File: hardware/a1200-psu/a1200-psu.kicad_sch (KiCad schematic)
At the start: 60 parts, among them J2 Conn_01x05, U1 PC817

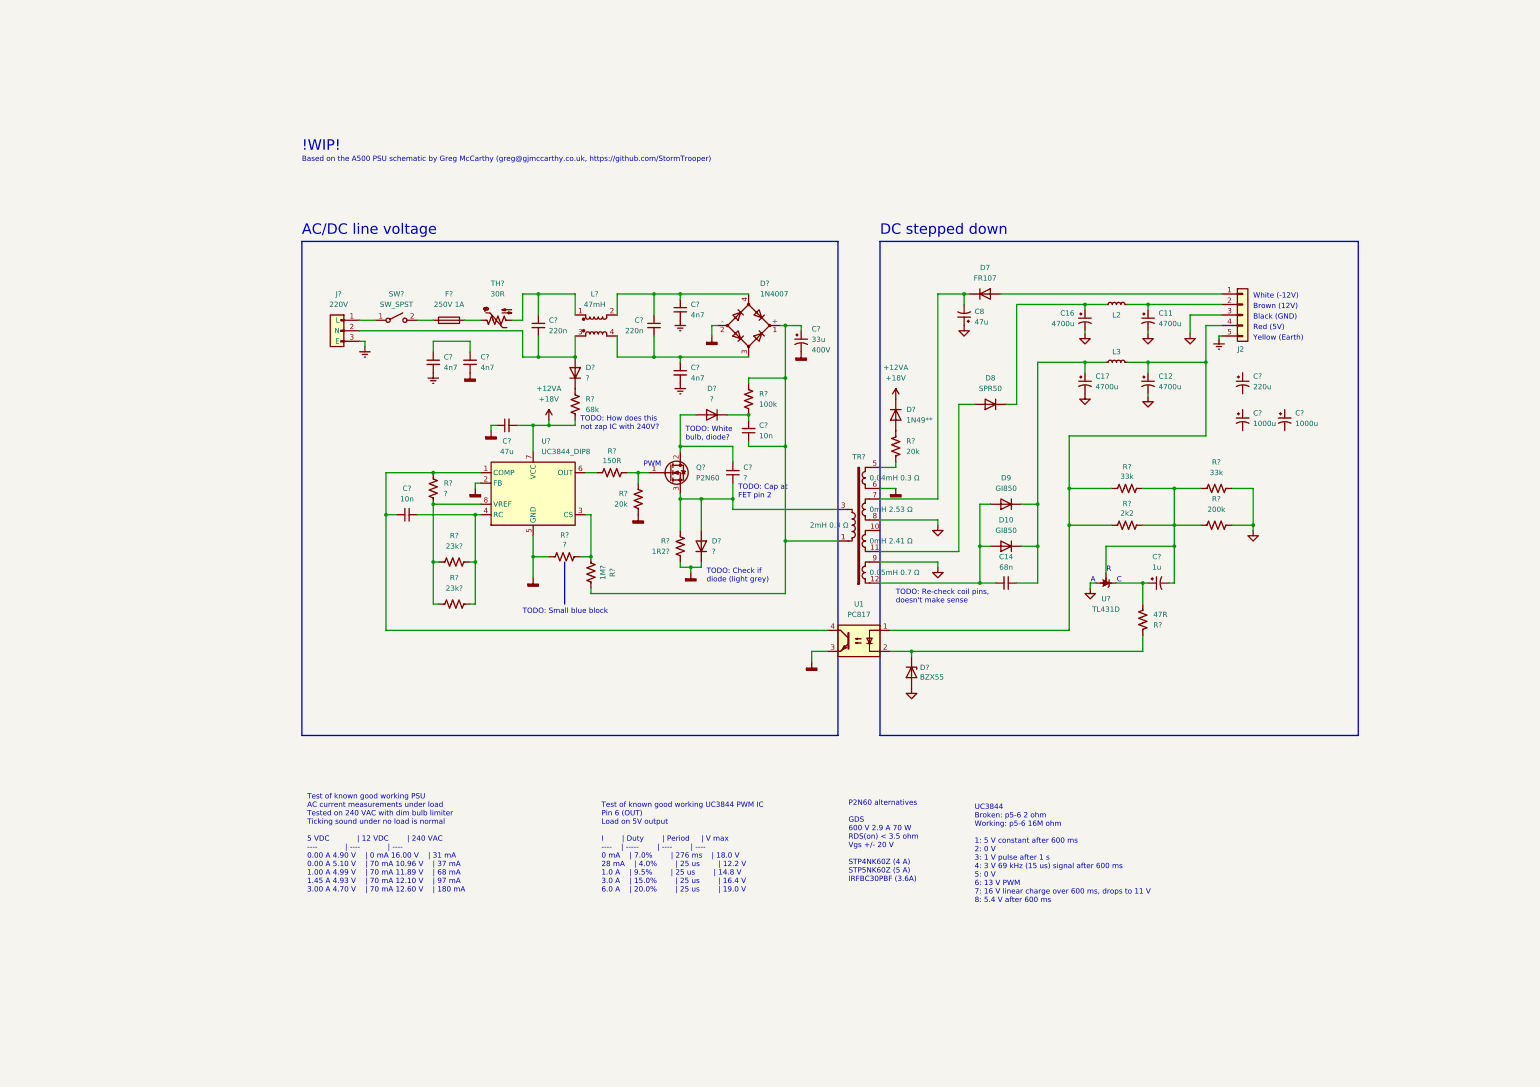
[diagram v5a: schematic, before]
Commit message: Fixed transformer wiring
Also corrected cap values
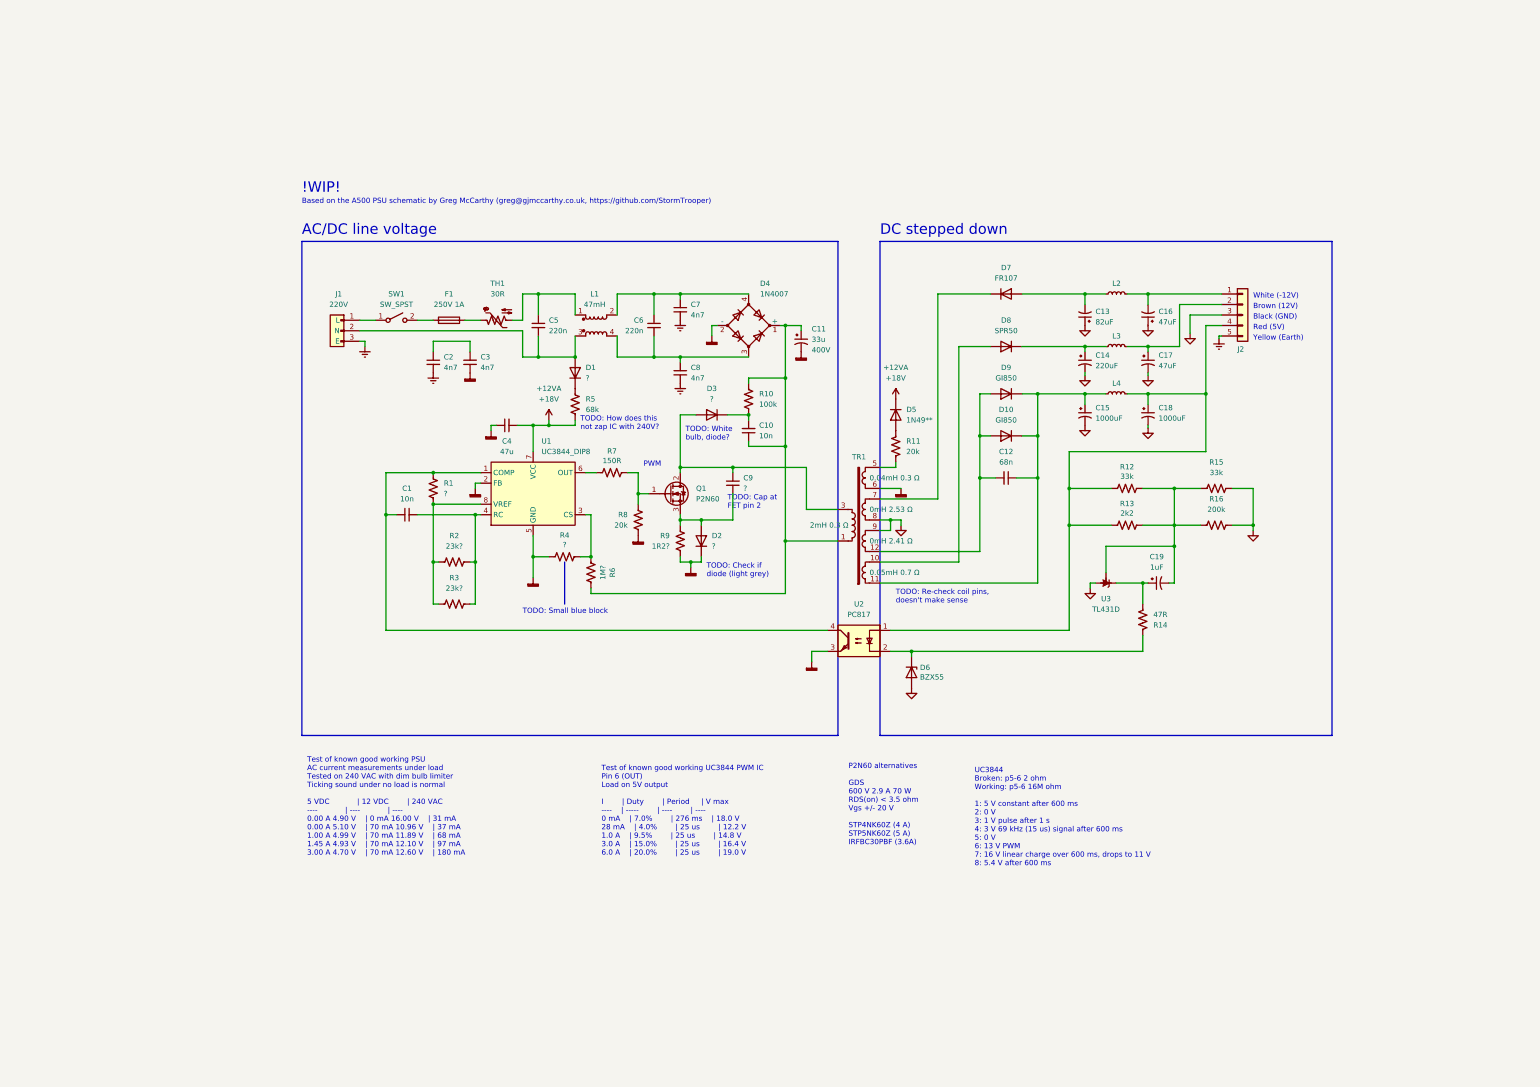
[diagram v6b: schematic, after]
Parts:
- removed C12, C17: 4700u, symbol a500-psu-rescue:CP1_Small-Device
- removed C8: 47u, symbol a500-psu-rescue:CP1_Small-Device
- removed C?: 220u, symbol a500-psu-rescue:CP1_Small-Device
- removed C? (x2): 1000u, symbol a500-psu-rescue:CP1_Small-Device
- added C13: 82uF, symbol a500-psu-rescue:CP1_Small-Device
- added C15, C18: 1000uF, symbol a500-psu-rescue:CP1_Small-Device
- added C16: 47uF, symbol a500-psu-rescue:CP1_Small-Device
- added L2: L_Small, symbol Device:L_Small
- C14: renamed from C16; value 4700u -> 220uF
- C17: renamed from C11; value 4700u -> 47uF
- C19: renamed from C?; value 1u -> 1uF
- U3: renamed from U?; symbol Reference_Voltage:TL431D -> Amiga 1200:TL431D
- gave numbers to parts that had none: 41
- renumbered C14 to C12, L2 to L3, L3 to L4, U1 to U2
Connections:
- net GND: now also C13.1, C15.2, C16.1, C18.2
- net at J2.1 (Pin_1): now also C16.2, L2.2; no longer D7.2 (A)
- net at J2.4 (Pin_4), L4.2, R12.2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: now also C18.1
- net at D8.2 (A): now also TR1.10; no longer TR1.11
- net at C12.1, D10.1 (K), D9.1 (K)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: now also TR1.11, C15.1
- net at C9.1, D2.2 (A), Q1.3 (S)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: no longer TR1.3
- net at C9.2, D3.2 (A), Q1.2 (D): now also TR1.3
- new net: C13.2, D7.2 (A), L2.1
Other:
- note removed: "A"
- note removed: "C"
- note removed: "R"
- title: Amiga A1200 PSU UK 391029-02 -> Amiga A1200 PSU (UK)
- moved on the sheet: C12, C14, C17, C9, D10, D2, D7, D8, D9, L3, L4, Q1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

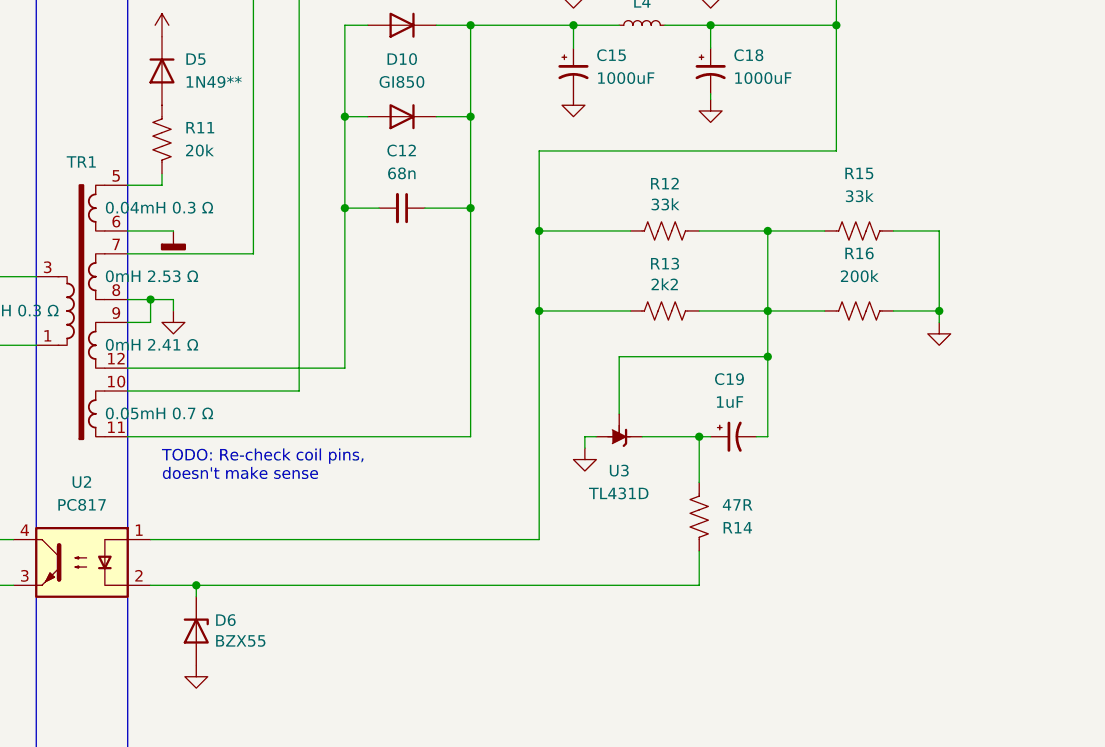
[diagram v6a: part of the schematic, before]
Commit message: Removed TR1 todo
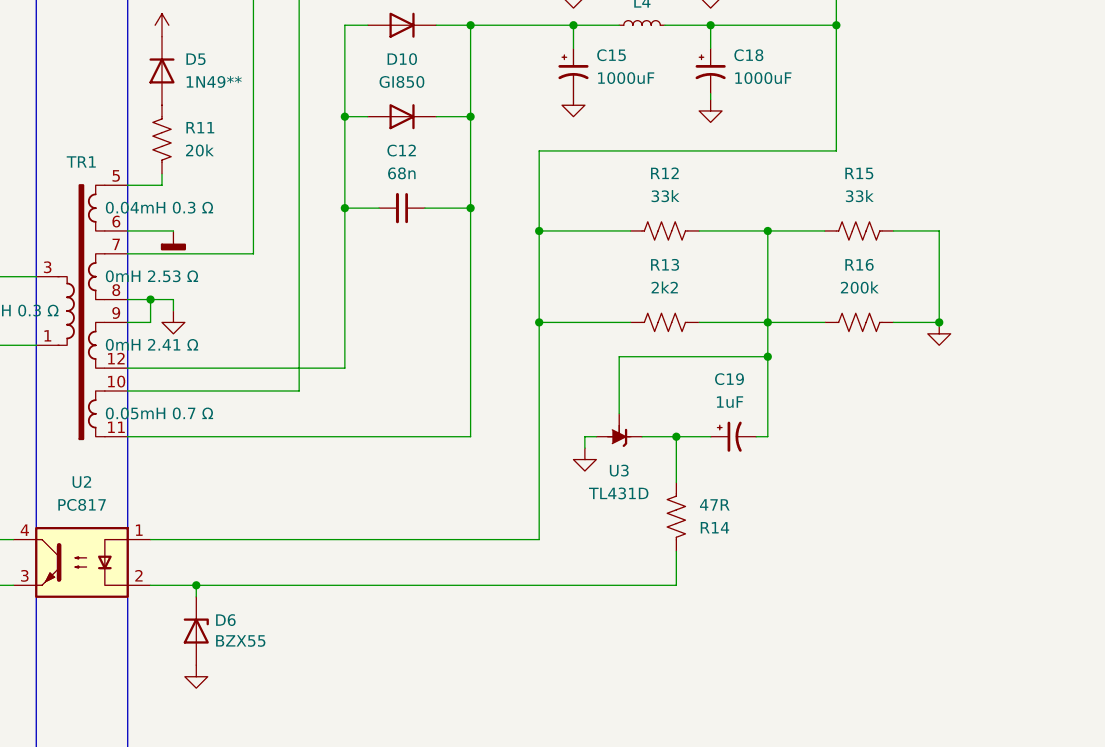
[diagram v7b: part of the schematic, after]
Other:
- note removed: "TODO: Re-check coil pins, doesn't make sense"
- moved on the sheet: R13, R14, R16
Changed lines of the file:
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@@
   (junction (at 304.8 106.68) (diameter 0) (color 0 0 0 0)
   )
-  (junction (at 271.78 138.43) (diameter 0) (color 0 0 0 0)
-  )
   (junction (at 118.11 147.32) (diameter 0) (color 0 0 0 0)
   )
   (junction (at 143.51 82.55) (diameter 0) (color 0 0 0 0)
   )
-  (junction (at 316.23 138.43) (diameter 0) (color 0 0 0 0)
-  )
   (junction (at 233.68 168.91) (diameter 0) (color 0 0 0 0)
   )
-  (junction (at 297.18 138.43) (diameter 0) (color 0 0 0 0)
-  )
   (junction (at 290.83 95.25) (diameter 0) (color 0 0 0 0)
   )
@@
   (junction (at 152.4 97.79) (diameter 0) (color 0 0 0 0)
   )
-  (junction (at 289.56 152.4) (diameter 0) (color 0 0 0 0)
-  )
   (junction (at 194.31 111.76) (diameter 0) (color 0 0 0 0)
   )
@@
   (junction (at 171.45 97.79) (diameter 0) (color 0 0 0 0)
   )
+  (junction (at 287.02 152.4) (diameter 0) (color 0 0 0 0)
+  )
+  (junction (at 271.78 139.7) (diameter 0) (color 0 0 0 0)
+  )
   (junction (at 297.18 129.54) (diameter 0) (color 0 0 0 0)
   )
+  (junction (at 316.23 139.7) (diameter 0) (color 0 0 0 0)
+  )
   (junction (at 177.8 97.79) (diameter 0) (color 0 0 0 0)
   )
+  (junction (at 297.18 139.7) (diameter 0) (color 0 0 0 0)
+  )
   (junction (at 177.8 82.55) (diameter 0) (color 0 0 0 0)
   )
@@
     (stroke (width 0) (type default) (color 0 0 0 0))
   )
-  (wire (pts (xy 289.56 138.43) (xy 297.18 138.43))
+  (wire (pts (xy 289.56 139.7) (xy 297.18 139.7))
     (stroke (width 0) (type default) (color 0 0 0 0))
   )
@@
     (stroke (width 0) (type default) (color 0 0 0 0))
   )
-  (wire (pts (xy 271.78 138.43) (xy 271.78 163.83))
-    (stroke (width 0) (type default) (color 0 0 0 0))
-  )
   (wire (pts (xy 240.03 82.55) (xy 252.73 82.55))
     (stroke (width 0) (type default) (color 0 0 0 0))
@@
     (stroke (width 0) (type default) (color 0 0 0 0))
   )
-  (wire (pts (xy 297.18 138.43) (xy 303.53 138.43))
+  (wire (pts (xy 297.18 139.7) (xy 303.53 139.7))
     (stroke (width 0) (type default) (color 0 0 0 0))
   )
@@
     (stroke (width 0) (type default) (color 0 0 0 0))
   )
+  (wire (pts (xy 271.78 139.7) (xy 271.78 163.83))
+    (stroke (width 0) (type default) (color 0 0 0 0))
+  )
   (wire (pts (xy 100.33 91.44) (xy 139.7 91.44))
     (stroke (width 0) (type default) (color 0 0 0 0))
@@
     (stroke (width 0) (type default) (color 0 0 0 0))
   )
-  (wire (pts (xy 316.23 129.54) (xy 316.23 138.43))
-    (stroke (width 0) (type default) (color 0 0 0 0))
-  )
   (wire (pts (xy 128.27 157.48) (xy 128.27 147.32))
     (stroke (width 0) (type default) (color 0 0 0 0))
@@
     (stroke (width 0) (type default) (color 0 0 0 0))
   )
-  (wire (pts (xy 289.56 157.48) (xy 289.56 152.4))
+  (wire (pts (xy 287.02 157.48) (xy 287.02 152.4))
     (stroke (width 0) (type default) (color 0 0 0 0))
   )
-  (wire (pts (xy 289.56 165.1) (xy 289.56 168.91))
+  (wire (pts (xy 287.02 165.1) (xy 287.02 168.91))
     (stroke (width 0) (type default) (color 0 0 0 0))
   )
@@
     (stroke (width 0) (type default) (color 0 0 0 0))
   )
-  (wire (pts (xy 316.23 139.7) (xy 316.23 138.43))
-    (stroke (width 0) (type default) (color 0 0 0 0))
-  )
   (wire (pts (xy 203.2 119.38) (xy 203.2 142.24))
     (stroke (width 0) (type default) (color 0 0 0 0))
@@
     (stroke (width 0) (type default) (color 0 0 0 0))
   )
+  (wire (pts (xy 297.18 139.7) (xy 297.18 143.51))
+    (stroke (width 0) (type default) (color 0 0 0 0))
+  )
   (wire (pts (xy 177.8 99.06) (xy 177.8 97.79))
     (stroke (width 0) (type default) (color 0 0 0 0))
@@
     (stroke (width 0) (type default) (color 0 0 0 0))
   )
-  (wire (pts (xy 283.21 152.4) (xy 289.56 152.4))
+  (wire (pts (xy 283.21 152.4) (xy 287.02 152.4))
     (stroke (width 0) (type default) (color 0 0 0 0))
   )
@@
     (stroke (width 0) (type default) (color 0 0 0 0))
   )
+  (wire (pts (xy 271.78 129.54) (xy 271.78 139.7))
+    (stroke (width 0) (type default) (color 0 0 0 0))
+  )
   (wire (pts (xy 118.11 125.73) (xy 129.54 125.73))
     (stroke (width 0) (type default) (color 0 0 0 0))
@@
     (stroke (width 0) (type default) (color 0 0 0 0))
   )
-  (wire (pts (xy 297.18 129.54) (xy 297.18 138.43))
+  (wire (pts (xy 297.18 129.54) (xy 297.18 139.7))
     (stroke (width 0) (type default) (color 0 0 0 0))
   )
@@
     (stroke (width 0) (type default) (color 0 0 0 0))
   )
+  (wire (pts (xy 316.23 129.54) (xy 316.23 139.7))
+    (stroke (width 0) (type default) (color 0 0 0 0))
+  )
   (wire (pts (xy 289.56 129.54) (xy 297.18 129.54))
     (stroke (width 0) (type default) (color 0 0 0 0))
@@
     (stroke (width 0) (type default) (color 0 0 0 0))
   )
-  (wire (pts (xy 271.78 129.54) (xy 271.78 138.43))
-    (stroke (width 0) (type default) (color 0 0 0 0))
-  )
   (wire (pts (xy 203.2 142.24) (xy 215.9 142.24))
     (stroke (width 0) (type default) (color 0 0 0 0))
@@
     (stroke (width 0) (type default) (color 0 0 0 0))
   )
-  (wire (pts (xy 289.56 152.4) (xy 290.83 152.4))
+  (wire (pts (xy 287.02 152.4) (xy 290.83 152.4))
     (stroke (width 0) (type default) (color 0 0 0 0))
   )
-  (wire (pts (xy 311.15 138.43) (xy 316.23 138.43))
+  (wire (pts (xy 311.15 139.7) (xy 316.23 139.7))
     (stroke (width 0) (type default) (color 0 0 0 0))
   )
@@
     (stroke (width 0) (type default) (color 0 0 0 0))
   )
-  (wire (pts (xy 271.78 138.43) (xy 281.94 138.43))
+  (wire (pts (xy 271.78 139.7) (xy 281.94 139.7))
     (stroke (width 0) (type default) (color 0 0 0 0))
   )
@@
     (stroke (width 0) (type default) (color 0 0 0 0))
   )
-  (wire (pts (xy 297.18 138.43) (xy 297.18 143.51))
-    (stroke (width 0) (type default) (color 0 0 0 0))
-  )
-  (wire (pts (xy 233.68 168.91) (xy 289.56 168.91))
+  (wire (pts (xy 233.68 168.91) (xy 287.02 168.91))
     (stroke (width 0) (type default) (color 0 0 0 0))
   )
@@
     (effects (font (size 1.27 1.27)) (justify left bottom))
   )
-  (text "TODO: Re-check coil pins, \ndoesn't make sense" (at 229.87 157.48 0)
-    (effects (font (size 1.27 1.27)) (justify left bottom))
-  )
   (text "UC3844\nBroken: p5-6 2 ohm\nWorking: p5-6 16M ohm\n\n1: 5 V constant after 600 ms\n2: 0 V\n3: 1 V pulse after 1 s\n4: 3 V 69 kHz (15 us) signal after 600 ms\n5: 0 V\n6: 13 V PWM\n7: 16 V linear charge over 600 ms, drops to 11 V\n8: 5.4 V after 600 ms"
     (at 248.92 220.98 0)
@@
   )
   (symbol (lib_id "Device:R_US") (at 285.75 129.54 270) (unit 1)
-    (in_bom yes) (on_board yes)
-    (property "Reference" "R12" (id 0) (at 285.75 124.333 90))
-    (property "Value" "33k" (id 1) (at 285.75 126.6444 90))
+    (in_bom yes) (on_board yes) (fields_autoplaced)
+    (property "Reference" "R12" (id 0) (at 285.75 123.19 90))
+    (property "Value" "33k" (id 1) (at 285.75 125.73 90))
     (property "Footprint" "" (id 2) (at 285.496 130.556 90)
       (effects (font (size 1.27 1.27)) hide)
@@
     (pin "8")
   )
-  (symbol (lib_id "Device:R_US") (at 289.56 161.29 0) (mirror y) (unit 1)
+  (symbol (lib_id "Device:R_US") (at 287.02 161.29 0) (mirror y) (unit 1)
     (in_bom yes) (on_board yes) (fields_autoplaced)
-    (property "Reference" "R14" (id 0) (at 292.1 162.5601 0)
+    (property "Reference" "R14" (id 0) (at 289.56 162.5601 0)
       (effects (font (size 1.27 1.27)) (justify right))
     )
-    (property "Value" "47R" (id 1) (at 292.1 160.0201 0)
+    (property "Value" "47R" (id 1) (at 289.56 160.0201 0)
       (effects (font (size 1.27 1.27)) (justify right))
     )
-    (property "Footprint" "" (id 2) (at 288.544 161.544 90)
+    (property "Footprint" "" (id 2) (at 286.004 161.544 90)
       (effects (font (size 1.27 1.27)) hide)
     )
-    (property "Datasheet" "~" (id 3) (at 289.56 161.29 0)
+    (property "Datasheet" "~" (id 3) (at 287.02 161.29 0)
       (effects (font (size 1.27 1.27)) hide)
     )
@@
     (pin "2")
   )
-  (symbol (lib_id "Device:R_US") (at 307.34 138.43 270) (unit 1)
+  (symbol (lib_id "Device:R_US") (at 307.34 139.7 270) (unit 1)
     (in_bom yes) (on_board yes) (fields_autoplaced)
-    (property "Reference" "R16" (id 0) (at 307.34 132.08 90))
-    (property "Value" "200k" (id 1) (at 307.34 134.62 90))
-    (property "Footprint" "" (id 2) (at 307.086 139.446 90)
+    (property "Reference" "R16" (id 0) (at 307.34 133.35 90))
+    (property "Value" "200k" (id 1) (at 307.34 135.89 90))
+    (property "Footprint" "" (id 2) (at 307.086 140.716 90)
       (effects (font (size 1.27 1.27)) hide)
     )
-    (property "Datasheet" "~" (id 3) (at 307.34 138.43 0)
+    (property "Datasheet" "~" (id 3) (at 307.34 139.7 0)
       (effects (font (size 1.27 1.27)) hide)
     )
@@
     (pin "1")
   )
-  (symbol (lib_id "Device:R_US") (at 285.75 138.43 270) (unit 1)
-    (in_bom yes) (on_board yes)
-    (property "Reference" "R13" (id 0) (at 285.75 133.223 90))
-    (property "Value" "2k2" (id 1) (at 285.75 135.5344 90))
-    (property "Footprint" "" (id 2) (at 285.496 139.446 90)
+  (symbol (lib_id "Device:R_US") (at 285.75 139.7 270) (unit 1)
+    (in_bom yes) (on_board yes) (fields_autoplaced)
+    (property "Reference" "R13" (id 0) (at 285.75 133.35 90))
+    (property "Value" "2k2" (id 1) (at 285.75 135.89 90))
+    (property "Footprint" "" (id 2) (at 285.496 140.716 90)
       (effects (font (size 1.27 1.27)) hide)
     )
-    (property "Datasheet" "~" (id 3) (at 285.75 138.43 0)
+    (property "Datasheet" "~" (id 3) (at 285.75 139.7 0)
       (effects (font (size 1.27 1.27)) hide)
     )
